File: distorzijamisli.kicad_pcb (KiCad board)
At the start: 2 copper layers, 107.3 x 92.7 mm, 138 parts, among them J1 SW DBG, J10 Audio-Jack-3, J11 MicBias, J12 5V, J2 USB_OTG, J3 Conn_02x16_Odd_Even, J4 Conn_02x16_Odd_Even, J5 Conn_02x08_Odd_Even, J6 Conn_02x03_Odd_Even, J7 Conn_02x03_Odd_Even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

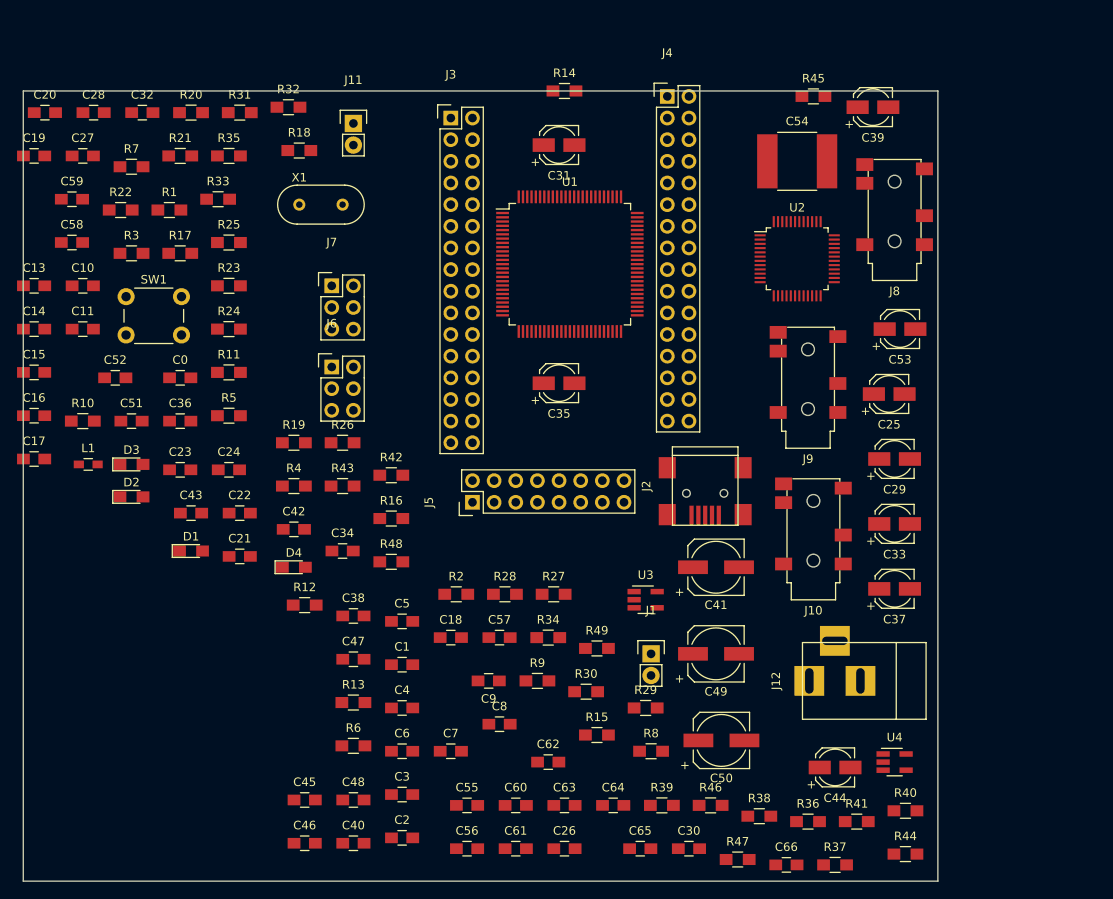
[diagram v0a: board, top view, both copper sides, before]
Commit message: Regenerated footprints for the new netlist
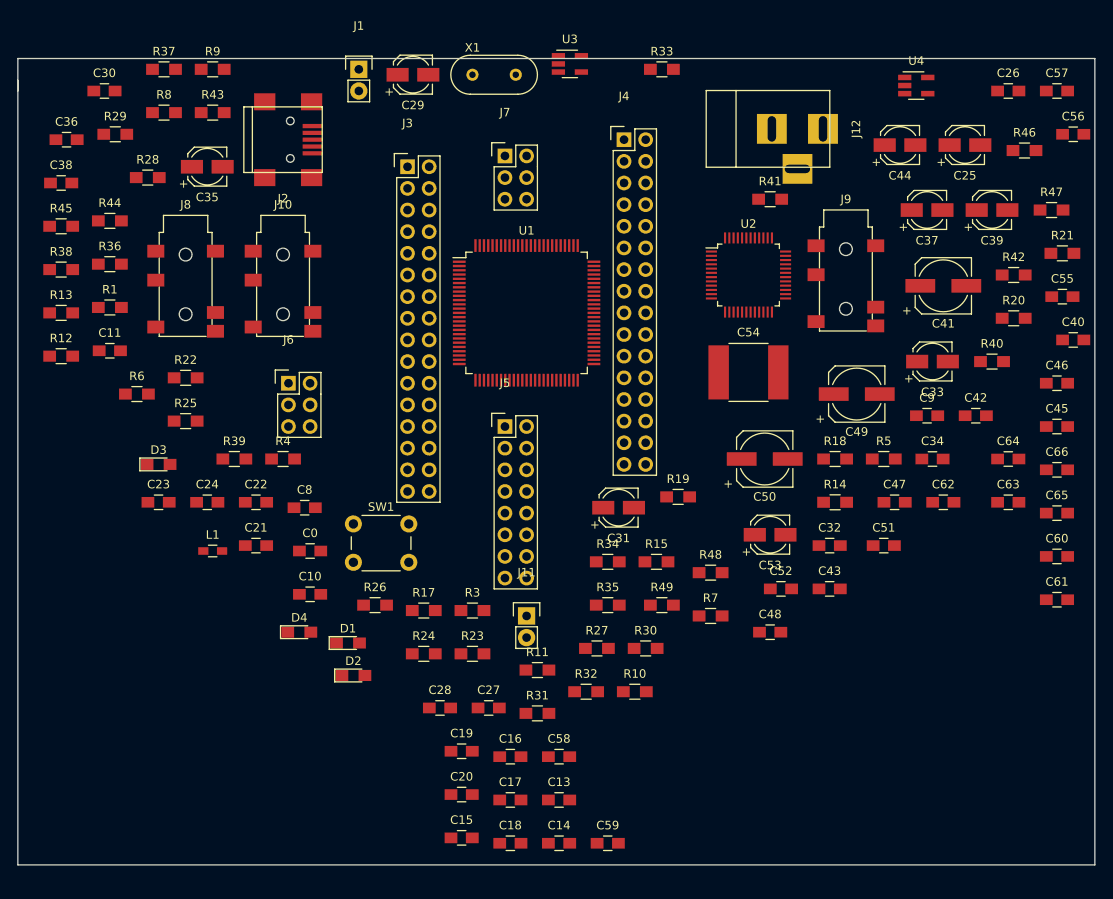
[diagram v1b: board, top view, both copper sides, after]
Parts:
- removed C1, C2, C3, C4, C5, C6: 100n, Capacitors_SMD:C_0805_HandSoldering
- removed C7: 1u, Capacitors_SMD:C_0805_HandSoldering
- removed R16, R2: 0, Resistors_SMD:R_0805_HandSoldering
- moved R37 122.1 mm to (40.6, 17.1)
- moved R44 119.3 mm to (34.3, 34.9)
- moved C30 112.3 mm to (33.7, 19.7)
- moved C56 109.9 mm to (147.3, 24.8)
- moved R36 104.8 mm to (34.3, 40.0)
- moved R21 104.1 mm to (146.1, 38.7)
- moved R38 104.0 mm to (28.6, 40.6)
- moved C46 103.5 mm to (145.4, 54.0)
- moved C40 103.1 mm to (147.3, 48.9)
- moved C26 103.0 mm to (139.7, 19.7)
- moved R20 99.5 mm to (140.3, 46.4)
- moved C45 98.5 mm to (145.4, 59.1)
- moved C59 98.3 mm to (92.7, 108.0)
- moved C32 95.3 mm to (118.7, 73.0)
- moved R8 94.2 mm to (40.6, 22.2)
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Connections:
- net /Vda renamed /Vref
- U1 pad 6: Net-(R16-Pad1) -> 3V
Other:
- board size 107.3 x 92.7 mm -> 126.4 x 94.6 mm
